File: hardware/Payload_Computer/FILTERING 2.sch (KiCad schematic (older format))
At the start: 4 parts

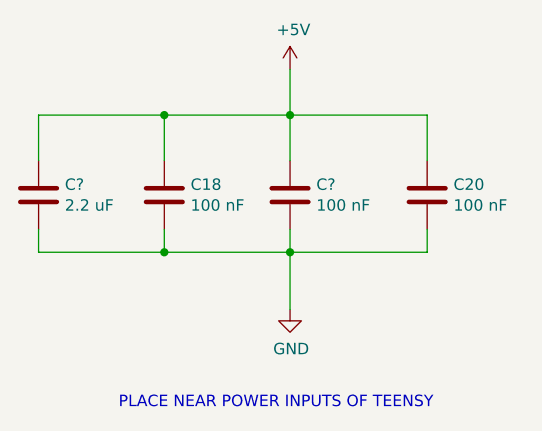
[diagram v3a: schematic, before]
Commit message: Finished Fan Schematic. Working on Servos
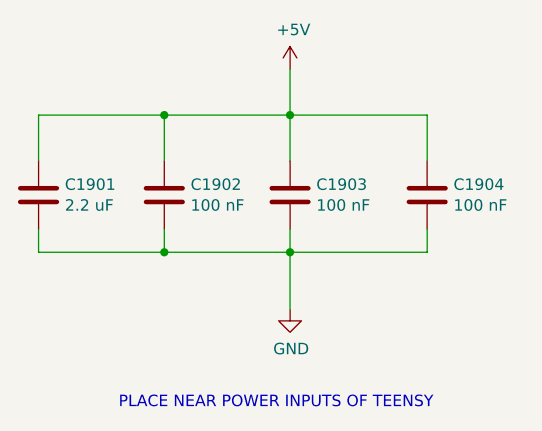
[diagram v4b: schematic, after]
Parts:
- C18, C20: footprint (none) -> Capacitor_SMD:C_0603_1608Metric_Pad1.08x0.95mm_HandSolder
- C601, C602: renamed from C?; footprint (none) -> Capacitor_SMD:C_0603_1608Metric_Pad1.08x0.95mm_HandSolder
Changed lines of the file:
@@
 $Descr A4 11693 8268
 encoding utf-8
-Sheet 26 26
+Sheet 19 22
 Title ""
 Date ""
@@
 P 5200 3750
 AR Path="/5F99419C/5F9988E5" Ref="C18"  Part="1"
-AR Path="/602AB697/5F9988E5" Ref="C?"  Part="1"
-F 0 "C?" H 5315 3796 50  0000 L CNN
+AR Path="/602AB697/5F9988E5" Ref="C1902"  Part="1"
+F 0 "C1902" H 5315 3796 50  0000 L CNN
 F 1 "100 nF" H 5315 3705 50  0000 L CNN
-F 2 "" H 5238 3600 50  0001 C CNN
+F 2 "Capacitor_SMD:C_0603_1608Metric_Pad1.08x0.95mm_HandSolder" H 5238 3600 50  0001 C CNN
 F 3 "~" H 5200 3750 50  0001 C CNN
 	1    5200 3750
@@
 P 6350 3750
 AR Path="/5F99419C/5F9988EB" Ref="C20"  Part="1"
-AR Path="/602AB697/5F9988EB" Ref="C?"  Part="1"
-F 0 "C?" H 6465 3796 50  0000 L CNN
+AR Path="/602AB697/5F9988EB" Ref="C1904"  Part="1"
+F 0 "C1904" H 6465 3796 50  0000 L CNN
 F 1 "100 nF" H 6465 3705 50  0000 L CNN
-F 2 "" H 6388 3600 50  0001 C CNN
+F 2 "Capacitor_SMD:C_0603_1608Metric_Pad1.08x0.95mm_HandSolder" H 6388 3600 50  0001 C CNN
 F 3 "~" H 6350 3750 50  0001 C CNN
 	1    6350 3750
@@
 P 5750 3200
 AR Path="/5F99419C/5F9988F7" Ref="#PWR0141"  Part="1"
-AR Path="/602AB697/5F9988F7" Ref="#PWR?"  Part="1"
-F 0 "#PWR?" H 5750 3050 50  0001 C CNN
+AR Path="/602AB697/5F9988F7" Ref="#PWR01901"  Part="1"
+F 0 "#PWR01901" H 5750 3050 50  0001 C CNN
 F 1 "+5V" H 5765 3373 50  0000 C CNN
 F 2 "" H 5750 3200 50  0001 C CNN
@@
 P 5750 4250
 AR Path="/5F99419C/5F9988FD" Ref="#PWR0142"  Part="1"
-AR Path="/602AB697/5F9988FD" Ref="#PWR?"  Part="1"
-F 0 "#PWR?" H 5750 4000 50  0001 C CNN
+AR Path="/602AB697/5F9988FD" Ref="#PWR01902"  Part="1"
+F 0 "#PWR01902" H 5750 4000 50  0001 C CNN
 F 1 "GND" H 5755 4077 50  0000 C CNN
 F 2 "" H 5750 4250 50  0001 C CNN
@@
 PLACE NEAR POWER INPUTS OF TEENSY \n\n\n
 $Comp
-L Device:C C?
+L Device:C C602
 U 1 1 5FC1F499
 P 5750 3750
-AR Path="/5F99419C/5FC1F499" Ref="C?"  Part="1"
-AR Path="/602AB697/5FC1F499" Ref="C?"  Part="1"
-F 0 "C?" H 5865 3796 50  0000 L CNN
+AR Path="/5F99419C/5FC1F499" Ref="C602"  Part="1"
+AR Path="/602AB697/5FC1F499" Ref="C1903"  Part="1"
+F 0 "C1903" H 5865 3796 50  0000 L CNN
 F 1 "100 nF" H 5865 3705 50  0000 L CNN
-F 2 "" H 5788 3600 50  0001 C CNN
+F 2 "Capacitor_SMD:C_0603_1608Metric_Pad1.08x0.95mm_HandSolder" H 5788 3600 50  0001 C CNN
 F 3 "~" H 5750 3750 50  0001 C CNN
 	1    5750 3750
@@
 $EndComp
 $Comp
-L Device:C C?
+L Device:C C601
 U 1 1 5FC1F8C7
 P 4650 3750
-AR Path="/5F99419C/5FC1F8C7" Ref="C?"  Part="1"
-AR Path="/602AB697/5FC1F8C7" Ref="C?"  Part="1"
-F 0 "C?" H 4765 3796 50  0000 L CNN
+AR Path="/5F99419C/5FC1F8C7" Ref="C601"  Part="1"
+AR Path="/602AB697/5FC1F8C7" Ref="C1901"  Part="1"
+F 0 "C1901" H 4765 3796 50  0000 L CNN
 F 1 "2.2 uF" H 4765 3705 50  0000 L CNN
-F 2 "" H 4688 3600 50  0001 C CNN
+F 2 "Capacitor_SMD:C_0603_1608Metric_Pad1.08x0.95mm_HandSolder" H 4688 3600 50  0001 C CNN
 F 3 "~" H 4650 3750 50  0001 C CNN
 	1    4650 3750

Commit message: More Routing Work
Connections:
- net +5V renamed +3V3
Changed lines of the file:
@@
 $Descr A4 11693 8268
 encoding utf-8
-Sheet 19 21
+Sheet 13 21
 Title ""
 Date ""
@@
 F 3 "~" H 6350 3750 50  0001 C CNN
 	1    6350 3750
-	1    0    0    -1
-$EndComp
-$Comp
-L power:+5V #PWR0141
-U 1 1 5F9988F7
-P 5750 3200
-AR Path="/5F99419C/5F9988F7" Ref="#PWR0141"  Part="1"
-AR Path="/602AB697/5F9988F7" Ref="#PWR01901"  Part="1"
-F 0 "#PWR01901" H 5750 3050 50  0001 C CNN
-F 1 "+5V" H 5765 3373 50  0000 C CNN
-F 2 "" H 5750 3200 50  0001 C CNN
-F 3 "" H 5750 3200 50  0001 C CNN
-	1    5750 3200
 	1    0    0    -1
 $EndComp
@@
 	4650 4000 5200 4000
 Connection ~ 5200 4000
+$Comp
+L power:+3.3V #PWR?
+U 1 1 603751C8
+P 5750 3200
+AR Path="/5F99419C/603751C8" Ref="#PWR?"  Part="1"
+AR Path="/602AB697/603751C8" Ref="#PWR?"  Part="1"
+F 0 "#PWR?" H 5750 3050 50  0001 C CNN
+F 1 "+3.3V" H 5765 3373 50  0000 C CNN
+F 2 "" H 5750 3200 50  0001 C CNN
+F 3 "" H 5750 3200 50  0001 C CNN
+	1    5750 3200
+	1    0    0    -1
+$EndComp
 $EndSCHEMATC
